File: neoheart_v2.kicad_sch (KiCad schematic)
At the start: 45 parts, among them J1 Conn_01x03, Q1 A1SHB, Q2 BSS138, Q3 A1SHB, U1 ATtiny816-MNR, U2 TPS61240TDRVRQ1

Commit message: board revision 2.1
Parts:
- removed Q3: A1SHB, lib:SOT95P237X112-3N, symbol IRLML2502:IRLML2502
- removed R6: 1K, Resistor_SMD:R_0603_1608Metric, symbol Device:R
- removed R7: 10K, Resistor_SMD:R_0603_1608Metric, symbol Device:R
- added TP1, TP2: PC3, TestPoint:TestPoint_Pad_D1.0mm, symbol Connector:TestPoint_Small
- renumbered U1 to MCU1
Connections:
- net +3V0: now also J1.3 (Pin_3), R1.1
- net +5V: now also TP2.1; no longer J1.3 (Pin_3), R1.1
- net LED_DATA: now also TP1.1
- net ADC_BAT: no longer names the net of MCU1.1 (PA2)
- net ADC_MOSFET: no longer names the net of MCU1.18 (PC3)
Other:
- note removed: "BATTERY VOLTAGE READER (ADC)"
- moved on the sheet: TP4

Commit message: revision 2.1, pcbway production files
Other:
- note added: "03/06/2024"
- note added: "V2.1"
- note removed: "06/05/2024"
- note removed: "V2"
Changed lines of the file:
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@@
 	(wire
 		(pts
-			(xy 171.45 113.03) (xy 176.53 113.03)
+			(xy 166.37 113.03) (xy 176.53 113.03)
 		)
 		(stroke
@@
 		)
 	)
-	(text "06/05/2024"
+	(text "03/06/2024"
 		(exclude_from_sim no)
 		(at 212.344 193.294 0)
@@
 		)
 	)
-	(text "V2"
+	(text "V2.1"
 		(exclude_from_sim no)
-		(at 269.748 193.294 0)
+		(at 270.256 193.548 0)
 		(effects
 			(font
@@
 	(symbol
 		(lib_id "power:+3V0")
-		(at 171.45 113.03 90)
+		(at 166.37 113.03 0)
 		(unit 1)
 		(exclude_from_sim no)
@@
 		(fields_autoplaced yes)
 		(property "Reference" "#PWR04"
-			(at 175.26 113.03 0)
+			(at 166.37 116.84 0)
 			(effects
 				(font
@@
 		)
 		(property "Value" "+3V0"
-			(at 167.64 113.0299 90)
+			(at 168.91 111.7599 0)
 			(effects
 				(font
@@
 		)
 		(property "Footprint" ""
-			(at 171.45 113.03 0)
+			(at 166.37 113.03 0)
 			(effects
 				(font
@@
 		)
 		(property "Datasheet" ""
-			(at 171.45 113.03 0)
+			(at 166.37 113.03 0)
 			(effects
 				(font
@@
 		)
 		(property "Description" ""
-			(at 171.45 113.03 0)
+			(at 166.37 113.03 0)
 			(effects
 				(font

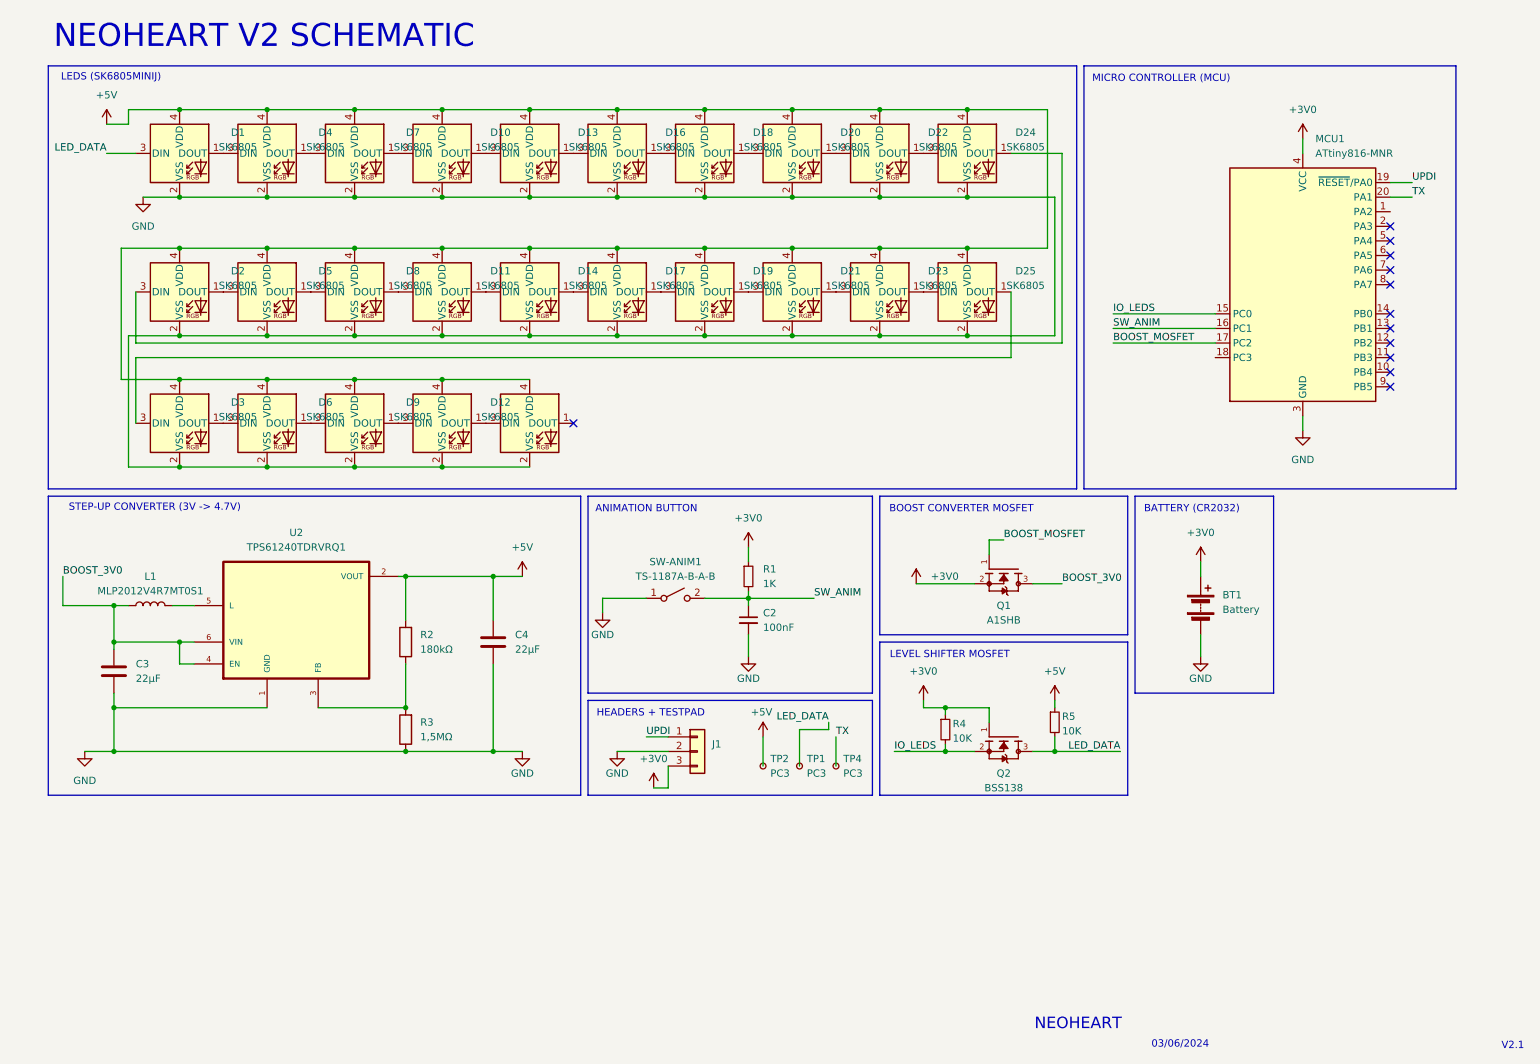
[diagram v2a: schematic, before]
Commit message: 2.2: update schematic, new boost converter design, hardware optimizations
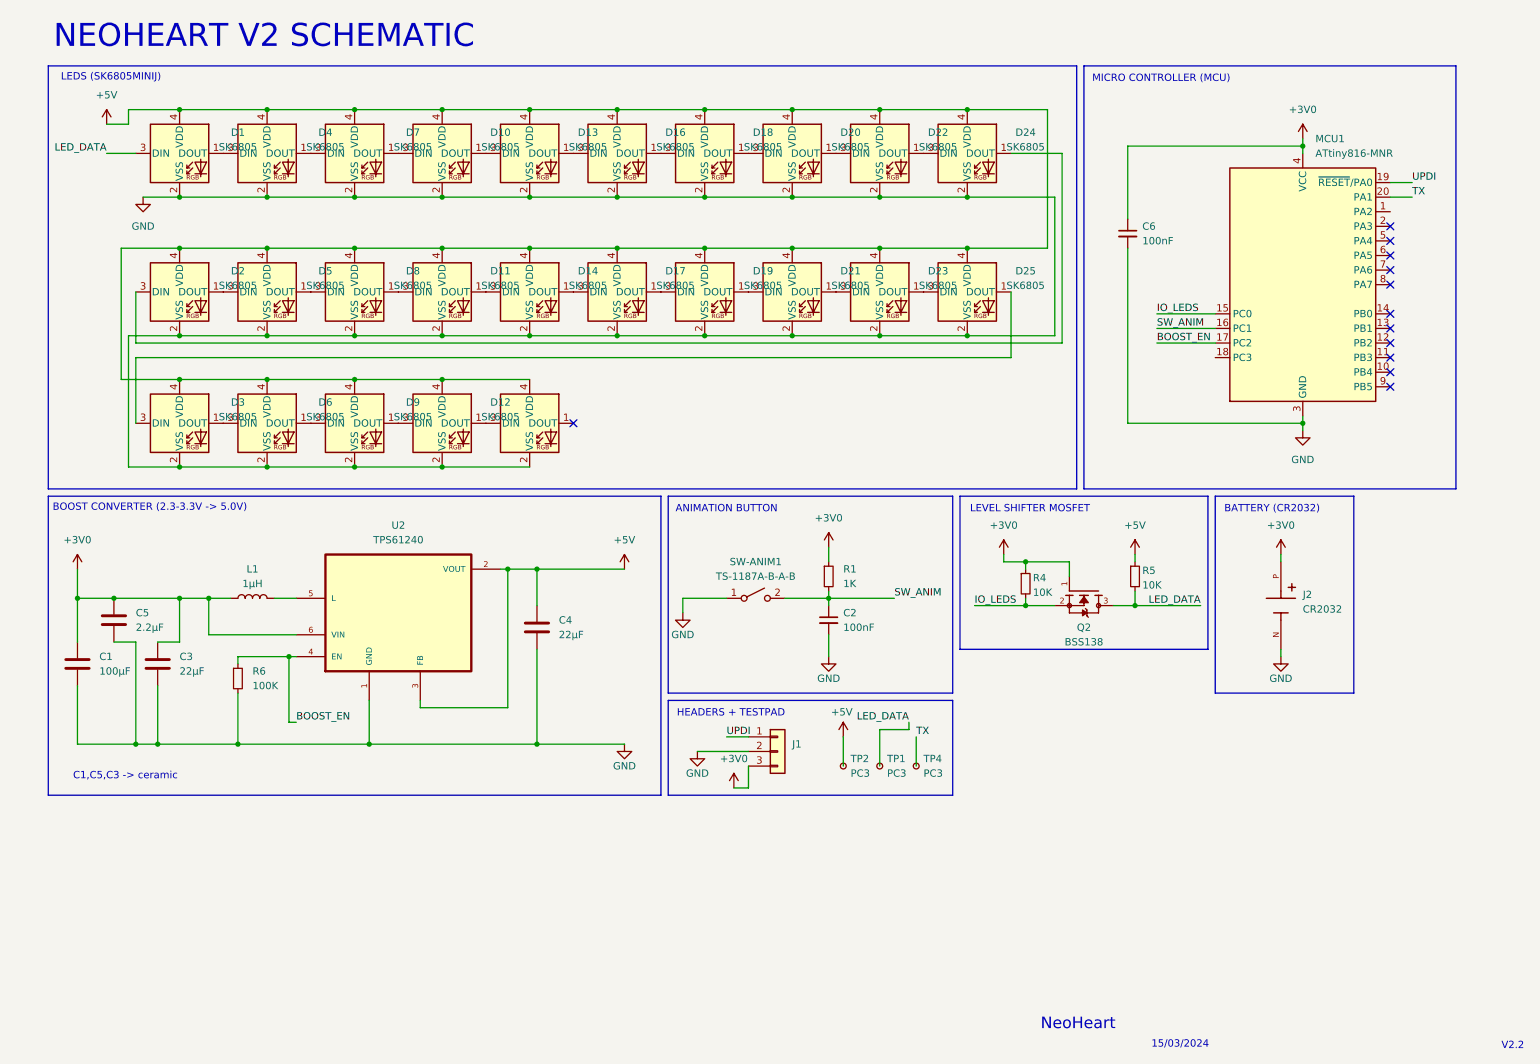
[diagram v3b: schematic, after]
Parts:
- removed BT1: Battery, Battery:BatteryHolder_Keystone_1060_1x2032, symbol Device:Battery
- removed Q1: A1SHB, lib:SOT95P237X112-3N, symbol IRLML2502:IRLML2502
- removed R2: 180kΩ, Resistor_SMD:R_0805_2012Metric, symbol Device:R
- removed R3: 1,5MΩ, Resistor_SMD:R_0603_1608Metric, symbol Device:R
- added C1: 100µF, Capacitor_SMD:C_1210_3225Metric_Pad1.33x2.70mm_HandSolder, symbol Device:C
- added C5: 2.2µF, Capacitor_SMD:C_0805_2012Metric_Pad1.18x1.45mm_HandSolder, symbol Device:C
- added C6: 100nF, Capacitor_SMD:C_0603_1608Metric, symbol Device:C_Small
- added J2: CR2032, lib:HARWIN_S8421-45R, symbol S8421-45R:S8421-45R
- added R6: 100K, Resistor_SMD:R_0805_2012Metric_Pad1.20x1.40mm_HandSolder, symbol Device:R_Small
- C3: footprint Capacitor_SMD:C_0603_1608Metric -> Capacitor_SMD:C_0805_2012Metric_Pad1.18x1.45mm_HandSolder
- C4: footprint Capacitor_SMD:C_0603_1608Metric -> Capacitor_SMD:C_0603_1608Metric_Pad1.08x0.95mm_HandSolder
- L1: value MLP2012V4R7MT0S1 -> 1μH; footprint Inductor_SMD:L_0805_2012Metric -> Inductor_SMD:L_0805_2012Metric_Pad1.05x1.20mm_HandSolder
- TP1, TP2, TP4: footprint TestPoint:TestPoint_Pad_D1.0mm -> TestPoint:TestPoint_Pad_D2.0mm
- U2: value TPS61240TDRVRQ1 -> TPS61240
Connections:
- net +3V0: now also C3.1, L1.1, U2.6 (VIN), C1.1, C5.1, C6.1, J2.P
- net +5V: now also U2.3 (FB)
- net GND: now also C1.2, C5.2, C6.2, J2.N, R6.2
- removed net BOOST_3V0: C3.1, L1.1, U2.4 (EN), U2.6 (VIN)
- net BOOST_MOSFET renamed BOOST_EN
- net BOOST_EN: now also U2.4 (EN), R6.1
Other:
- note added: "15/03/2024"
- note added: "BOOST CONVERTER (2.3-3.3V -> 5.0V)"
- note added: "C1,C5,C3 -> ceramic"
- note added: "NeoHeart"
- note added: "V2.2"
- note removed: "03/06/2024"
- note removed: "BOOST CONVERTER MOSFET"
- note removed: "NEOHEART"
- note removed: "STEP-UP CONVERTER (3V -> 4.7V)"
- note removed: "V2.1"
- moved on the sheet: C2, C4, J1, L1, Q2, R1, R4, R5, SW-ANIM1, TP1, TP2, TP4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

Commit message: 2.2: update PCB, add production files, new board renders
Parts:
- TP1, TP2, TP4: footprint TestPoint:TestPoint_Pad_D2.0mm -> TestPoint:TestPoint_Pad_D1.5mm
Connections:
- no-connect marks 12 -> 14
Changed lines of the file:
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@@
 	)
 	(no_connect
+		(at 218.44 73.66)
+	)
+	(no_connect
 		(at 106.68 85.09)
 	)
 	(no_connect
+		(at 248.92 48.26)
+	)
+	(no_connect
 		(at 248.92 58.42)
 	)
@@
 			)
 		)
-		(property "Datasheet" "~"
+		(property "Datasheet" "6.3 or 10V"
 			(at 20.32 127 0)
 			(effects
@@
 			)
 		)
-		(property "Footprint" "TestPoint:TestPoint_Pad_D2.0mm"
+		(property "Footprint" "TestPoint:TestPoint_Pad_D1.5mm"
 			(at 165.1 144.78 0)
 			(effects
@@
 			)
 		)
-		(property "Datasheet" "~"
+		(property "Datasheet" "6.3 or 10V"
 			(at 26.67 119.38 0)
 			(effects
@@
 			)
 		)
-		(property "Datasheet" "~"
+		(property "Datasheet" "ripple < 20%, at least 400mA"
 			(at 50.8 115.57 0)
 			(effects
@@
 			)
 		)
-		(property "Datasheet" "~"
+		(property "Datasheet" "6.3 or 10V"
 			(at 203.2 52.07 0)
 			(effects
@@
 			)
 		)
-		(property "Datasheet" "~"
+		(property "Datasheet" "10V"
 			(at 100.33 120.65 0)
 			(effects
@@
 			)
 		)
-		(property "Datasheet" "~"
+		(property "Datasheet" "6.3 or 10V"
 			(at 34.29 127 0)
 			(effects
@@
 			)
 		)
-		(property "Footprint" "TestPoint:TestPoint_Pad_D2.0mm"
+		(property "Footprint" "TestPoint:TestPoint_Pad_D1.5mm"
 			(at 171.45 144.78 0)
 			(effects
@@
 			)
 		)
-		(property "Footprint" "TestPoint:TestPoint_Pad_D2.0mm"
+		(property "Footprint" "TestPoint:TestPoint_Pad_D1.5mm"
 			(at 158.75 144.78 0)
 			(effects

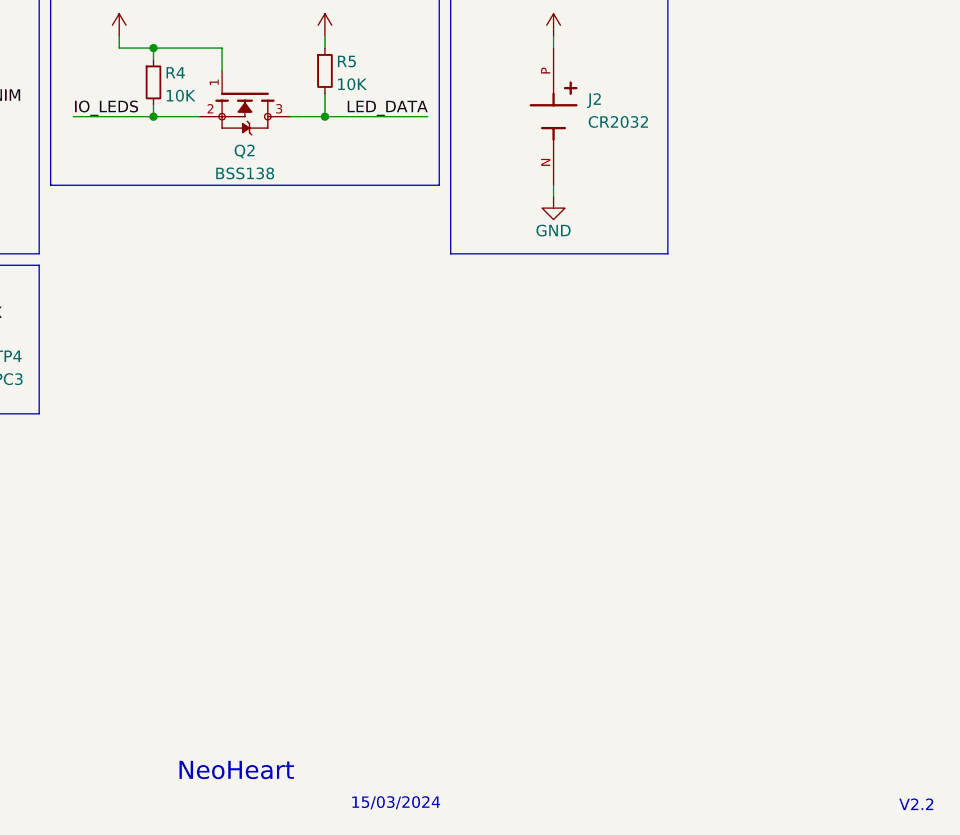
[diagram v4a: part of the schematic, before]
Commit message: change level shifter mosfet
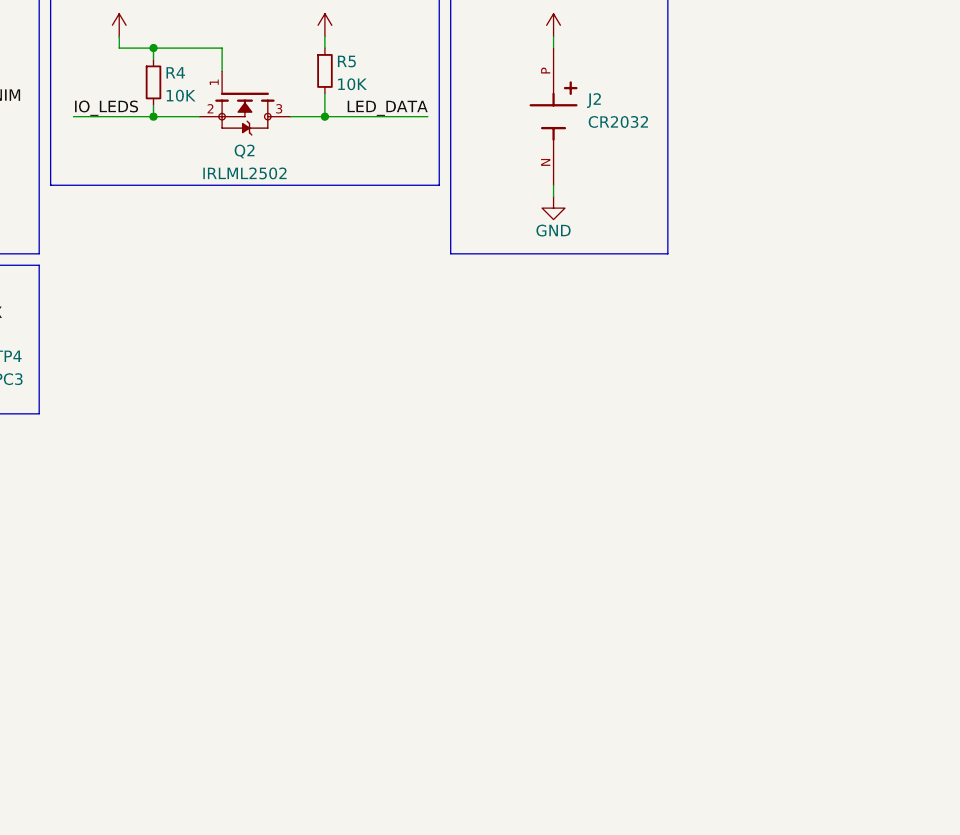
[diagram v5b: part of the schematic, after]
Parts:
- Q2: value BSS138 -> IRLML2502; Availability In Stock -> (none); Check_prices https://www.snapeda.com/parts/IRLML2502/Infineon+Technologi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 -> (none); MANUFACTURER Infineon Technologies -> (none); MAXIMUM_PACKAGE_HEIGHT 1.12 mm -> (none); MP IRLML2502 -> (none); PARTREV April 24, 2014 -> (none); Price None -> (none); Purchase-URL https://www.snapeda.com/api/url_track_click_mouser/?unipart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 -> (none); SNAPEDA_PACKAGE_ID 11907 -> (none); STANDARD IPC 7351B -> (none); SnapEDA_Link https://www.snapeda.com/parts/IRLML2502/Infineon+Technologi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 -> (none)
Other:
- note removed: "15/03/2024"
- note removed: "NeoHeart"
- note removed: "V2.2"
- company: (none) -> jack0217.dev
- title: (none) -> NeoHeart V2
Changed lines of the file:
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@@
 	(generator_version "9.0")
 	(paper "A4")
+	(title_block
+		(title "NeoHeart V2")
+		(date "2025-05-11")
+		(rev "2.2.1")
+		(company "jack0217.dev")
+	)
 	(text "MICRO CONTROLLER (MCU)"
 		(exclude_from_sim no)
@@
 		)
 	)
-	(text "NeoHeart"
-		(exclude_from_sim no)
-		(at 194.564 189.738 0)
-		(effects
-			(font
-				(size 2 2)
-			)
-		)
-	)
 	(text "HEADERS + TESTPAD"
 		(exclude_from_sim no)
@@
 		)
 	)
-	(text "15/03/2024"
-		(exclude_from_sim no)
-		(at 212.344 193.294 0)
-		(effects
-			(font
-				(size 1.27 1.27)
-			)
-		)
-	)
 	(text "LEDS (SK6805MINIJ)"
 		(exclude_from_sim no)
@@
 		)
 	)
-	(text "V2.2"
-		(exclude_from_sim no)
-		(at 270.256 193.548 0)
-		(effects
-			(font
-				(size 1.27 1.27)
-			)
-		)
-	)
 	(text "LEVEL SHIFTER MOSFET"
 		(exclude_from_sim no)
@@
 			)
 		)
-		(property "Value" "BSS138"
+		(property "Value" "IRLML2502"
 			(at 195.58 123.19 90)
 			(effects
@@
 			)
 		)
-		(property "Description" "\nN-Channel 20 V 4.2A (Ta) 1.25W (Ta) Surface Mount Micro3â„¢ /SOT-23\n"
+		(property "Description" "N-Channel 20 V 4.2A (Ta) 1.25W (Ta) Surface Mount Micro3â„¢ /SOT-23"
 			(at 195.58 114.3 0)
 			(effects
@@
 			)
 		)
-		(property "MAXIMUM_PACKAGE_HEIGHT" "1.12 mm"
-			(at 195.58 114.3 0)
-			(effects
-				(font
-					(size 1.27 1.27)
-				)
-				(justify bottom)
-				(hide yes)
-			)
-		)
 		(property "Package" "SOT-23-3 International Rectifier"
 			(at 195.58 114.3 0)
@@
 			)
 		)
-		(property "Price" "None"
-			(at 195.58 114.3 0)
-			(effects
-				(font
-					(size 1.27 1.27)
-				)
-				(justify bottom)
-				(hide yes)
-			)
-		)
-		(property "Check_prices" "https://www.snapeda.com/parts/IRLML2502/Infineon+Technologies/view-part/?ref=eda"
-			(at 195.58 114.3 0)
-			(effects
-				(font
-					(size 1.27 1.27)
-				)
-				(justify bottom)
-				(hide yes)
-			)
-		)
-		(property "STANDARD" "IPC 7351B"
-			(at 195.58 114.3 0)
-			(effects
-				(font
-					(size 1.27 1.27)
-				)
-				(justify bottom)
-				(hide yes)
-			)
-		)
-		(property "PARTREV" "April 24, 2014"
-			(at 195.58 114.3 0)
-			(effects
-				(font
-					(size 1.27 1.27)
-				)
-				(justify bottom)
-				(hide yes)
-			)
-		)
-		(property "SnapEDA_Link" "https://www.snapeda.com/parts/IRLML2502/Infineon+Technologies/view-part/?ref=snap"
-			(at 195.58 114.3 0)
-			(effects
-				(font
-					(size 1.27 1.27)
-				)
-				(justify bottom)
-				(hide yes)
-			)
-		)
-		(property "SNAPEDA_PACKAGE_ID" "11907"
-			(at 195.58 114.3 0)
-			(effects
-				(font
-					(size 1.27 1.27)
-				)
-				(justify bottom)
-				(hide yes)
-			)
-		)
-		(property "MP" "IRLML2502"
-			(at 195.58 114.3 0)
-			(effects
-				(font
-					(size 1.27 1.27)
-				)
-				(justify bottom)
-				(hide yes)
-			)
-		)
-		(property "Purchase-URL" "https://www.snapeda.com/api/url_track_click_mouser/?unipart_id=453707&manufacturer=Infineon Technologies&part_name=IRLML2502&search_term=None"
-			(at 195.58 114.3 0)
-			(effects
-				(font
-					(size 1.27 1.27)
-				)
-				(justify bottom)
-				(hide yes)
-			)
-		)
 		(property "SNAPEDA_PN" "IRLML2502"
 			(at 195.58 114.3 0)
 			(effects
-				(font
-					(size 1.27 1.27)
-				)
-				(justify bottom)
-				(hide yes)
-			)
-		)
-		(property "Availability" "In Stock"
-			(at 195.58 114.3 0)
-			(effects
-				(font
-					(size 1.27 1.27)
-				)
-				(justify bottom)
-				(hide yes)
-			)
-		)
-		(property "MANUFACTURER" "Infineon Technologies"
-			(at 195.58 114.3 0)
-			(effects
